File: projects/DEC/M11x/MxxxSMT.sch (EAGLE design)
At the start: 53 parts

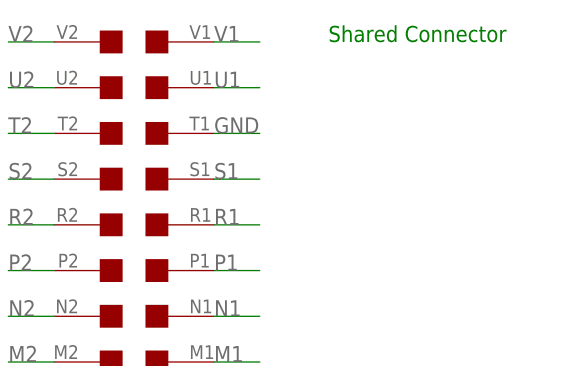
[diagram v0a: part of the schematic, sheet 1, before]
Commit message: Fix projects using THRU-HOLE2 to match new footprints.
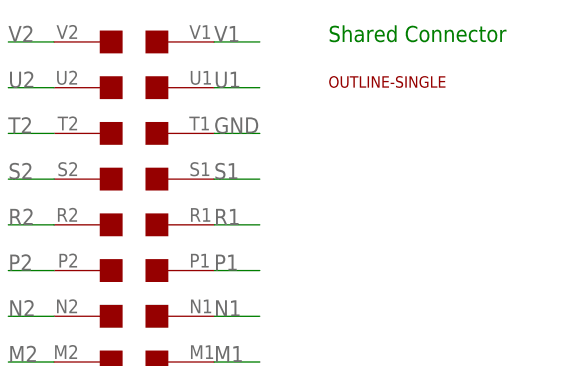
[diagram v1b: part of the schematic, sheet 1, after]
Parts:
- added U$4: OUTLINE-SINGLE, dec-con:OUTLINE-SINGLE
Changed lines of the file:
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@@
 <grid distance="0.1" unitdist="inch" unit="inch" style="lines" multiple="1" display="no" altdistance="0.01" altunitdist="inch" altunit="inch"/>
 <layers>
-<layer number="1" name="Top" color="4" fill="1" visible="yes" active="no"/>
-<layer number="2" name="Route2" color="1" fill="3" visible="yes" active="no"/>
-<layer number="3" name="Route3" color="4" fill="3" visible="yes" active="no"/>
-<layer number="4" name="Route4" color="1" fill="4" visible="yes" active="no"/>
-<layer number="5" name="Route5" color="4" fill="4" visible="yes" active="no"/>
-<layer number="6" name="Route6" color="1" fill="8" visible="yes" active="no"/>
-<layer number="7" name="Route7" color="4" fill="8" visible="yes" active="no"/>
-<layer number="8" name="Route8" color="1" fill="2" visible="yes" active="no"/>
-<layer number="9" name="Route9" color="4" fill="2" visible="yes" active="no"/>
-<layer number="10" name="Route10" color="1" fill="7" visible="yes" active="no"/>
-<layer number="11" name="Route11" color="4" fill="7" visible="yes" active="no"/>
-<layer number="12" name="Route12" color="1" fill="5" visible="yes" active="no"/>
-<layer number="13" name="Route13" color="4" fill="5" visible="yes" active="no"/>
-<layer number="14" name="Route14" color="1" fill="6" visible="yes" active="no"/>
-<layer number="15" name="Route15" color="4" fill="6" visible="yes" active="no"/>
-<layer number="16" name="Bottom" color="1" fill="1" visible="yes" active="no"/>
-<layer number="17" name="Pads" color="2" fill="1" visible="yes" active="no"/>
-<layer number="18" name="Vias" color="2" fill="1" visible="yes" active="no"/>
-<layer number="19" name="Unrouted" color="6" fill="1" visible="yes" active="no"/>
-<layer number="20" name="Dimension" color="15" fill="1" visible="yes" active="no"/>
-<layer number="21" name="tPlace" color="7" fill="1" visible="yes" active="no"/>
-<layer number="22" name="bPlace" color="7" fill="1" visible="yes" active="no"/>
-<layer number="23" name="tOrigins" color="15" fill="1" visible="yes" active="no"/>
-<layer number="24" name="bOrigins" color="15" fill="1" visible="yes" active="no"/>
-<layer number="25" name="tNames" color="7" fill="1" visible="yes" active="no"/>
-<layer number="26" name="bNames" color="7" fill="1" visible="yes" active="no"/>
-<layer number="27" name="tValues" color="7" fill="1" visible="yes" active="no"/>
-<layer number="28" name="bValues" color="7" fill="1" visible="yes" active="no"/>
+<layer number="1" name="Top" color="4" fill="1" visible="no" active="no"/>
+<layer number="2" name="Route2" color="1" fill="3" visible="no" active="no"/>
+<layer number="3" name="Route3" color="4" fill="3" visible="no" active="no"/>
+<layer number="4" name="Route4" color="1" fill="4" visible="no" active="no"/>
+<layer number="5" name="Route5" color="4" fill="4" visible="no" active="no"/>
+<layer number="6" name="Route6" color="1" fill="8" visible="no" active="no"/>
+<layer number="7" name="Route7" color="4" fill="8" visible="no" active="no"/>
+<layer number="8" name="Route8" color="1" fill="2" visible="no" active="no"/>
+<layer number="9" name="Route9" color="4" fill="2" visible="no" active="no"/>
+<layer number="10" name="Route10" color="1" fill="7" visible="no" active="no"/>
+<layer number="11" name="Route11" color="4" fill="7" visible="no" active="no"/>
+<layer number="12" name="Route12" color="1" fill="5" visible="no" active="no"/>
+<layer number="13" name="Route13" color="4" fill="5" visible="no" active="no"/>
+<layer number="14" name="Route14" color="1" fill="6" visible="no" active="no"/>
+<layer number="15" name="Route15" color="4" fill="6" visible="no" active="no"/>
+<layer number="16" name="Bottom" color="1" fill="1" visible="no" active="no"/>
+<layer number="17" name="Pads" color="2" fill="1" visible="no" active="no"/>
+<layer number="18" name="Vias" color="2" fill="1" visible="no" active="no"/>
+<layer number="19" name="Unrouted" color="6" fill="1" visible="no" active="no"/>
+<layer number="20" name="Dimension" color="15" fill="1" visible="no" active="no"/>
+<layer number="21" name="tPlace" color="7" fill="1" visible="no" active="no"/>
+<layer number="22" name="bPlace" color="7" fill="1" visible="no" active="no"/>
+<layer number="23" name="tOrigins" color="15" fill="1" visible="no" active="no"/>
+<layer number="24" name="bOrigins" color="15" fill="1" visible="no" active="no"/>
+<layer number="25" name="tNames" color="7" fill="1" visible="no" active="no"/>
+<layer number="26" name="bNames" color="7" fill="1" visible="no" active="no"/>
+<layer number="27" name="tValues" color="7" fill="1" visible="no" active="no"/>
+<layer number="28" name="bValues" color="7" fill="1" visible="no" active="no"/>
 <layer number="29" name="tStop" color="7" fill="3" visible="no" active="no"/>
 <layer number="30" name="bStop" color="7" fill="6" visible="no" active="no"/>
@@
 <layer number="35" name="tGlue" color="7" fill="4" visible="no" active="no"/>
 <layer number="36" name="bGlue" color="7" fill="5" visible="no" active="no"/>
-<layer number="37" name="tTest" color="7" fill="1" visible="yes" active="no"/>
-<layer number="38" name="bTest" color="7" fill="1" visible="yes" active="no"/>
+<layer number="37" name="tTest" color="7" fill="1" visible="no" active="no"/>
+<layer number="38" name="bTest" color="7" fill="1" visible="no" active="no"/>
 <layer number="39" name="tKeepout" color="4" fill="11" visible="no" active="no"/>
 <layer number="40" name="bKeepout" color="1" fill="11" visible="no" active="no"/>
@@
 <layer number="44" name="Drills" color="7" fill="1" visible="no" active="no"/>
 <layer number="45" name="Holes" color="7" fill="1" visible="no" active="no"/>
-<layer number="46" name="Milling" color="3" fill="1" visible="yes" active="no"/>
-<layer number="47" name="Measures" color="7" fill="1" visible="yes" active="no"/>
-<layer number="48" name="Document" color="7" fill="1" visible="yes" active="no"/>
-<layer number="49" name="Reference" color="7" fill="1" visible="yes" active="no"/>
-<layer number="50" name="dxf" color="7" fill="1" visible="yes" active="no"/>
-<layer number="51" name="tDocu" color="7" fill="1" visible="yes" active="no"/>
-<layer number="52" name="bDocu" color="7" fill="1" visible="yes" active="no"/>
-<layer number="53" name="tGND_GNDA" color="7" fill="1" visible="yes" active="no"/>
-<layer number="54" name="bGND_GNDA" color="7" fill="1" visible="yes" active="no"/>
-<layer number="56" name="wert" color="7" fill="1" visible="yes" active="no"/>
+<layer number="46" name="Milling" color="3" fill="1" visible="no" active="no"/>
+<layer number="47" name="Measures" color="7" fill="1" visible="no" active="no"/>
+<layer number="48" name="Document" color="7" fill="1" visible="no" active="no"/>
+<layer number="49" name="Reference" color="7" fill="1" visible="no" active="no"/>
+<layer number="50" name="dxf" color="7" fill="1" visible="no" active="no"/>
+<layer number="51" name="tDocu" color="7" fill="1" visible="no" active="no"/>
+<layer number="52" name="bDocu" color="7" fill="1" visible="no" active="no"/>
+<layer number="53" name="tGND_GNDA" color="7" fill="1" visible="no" active="no"/>
+<layer number="54" name="bGND_GNDA" color="7" fill="1" visible="no" active="no"/>
+<layer number="56" name="wert" color="7" fill="1" visible="no" active="no"/>
 <layer number="91" name="Nets" color="2" fill="1" visible="yes" active="yes"/>
 <layer number="92" name="Busses" color="1" fill="1" visible="yes" active="yes"/>
@@
 <part name="E20" library="74xx-us" deviceset="74*73" device="D" technology="LS" value="7473D"/>
 <part name="E21" library="74xx-us" deviceset="74*73" device="D" technology="LS" value="7473D"/>
+<part name="U$4" library="dec-con" deviceset="OUTLINE-*" device="SINGLE"/>
 </parts>
 <sheets>
@@
 <instance part="U$1" gate="B1" x="22.86" y="10.16" rot="MR0"/>
 <instance part="U$1" gate="A1" x="22.86" y="5.08" rot="MR0"/>
+<instance part="U$4" gate="G$1" x="38.1" y="86.36"/>
 </instances>
 <busses>
